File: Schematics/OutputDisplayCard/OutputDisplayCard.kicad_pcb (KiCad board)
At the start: 2 copper layers, 13 parts, among them U1 74LS393, U2 74LS32, U3 74F377, U4 74LS139, U5 74LS245, U6 GLS29EE010, U7 CC56-12CGKWA

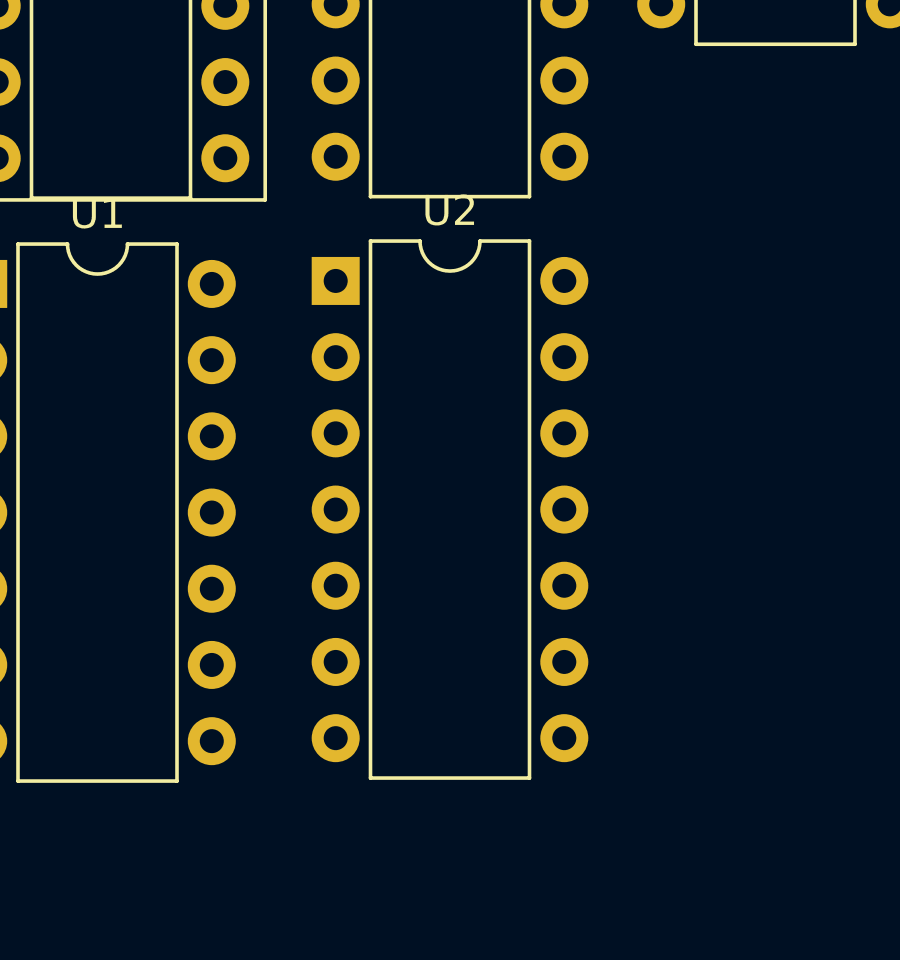
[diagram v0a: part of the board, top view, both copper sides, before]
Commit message: Update schematics for OutputDisplayCard to include the new PI and PO signals.
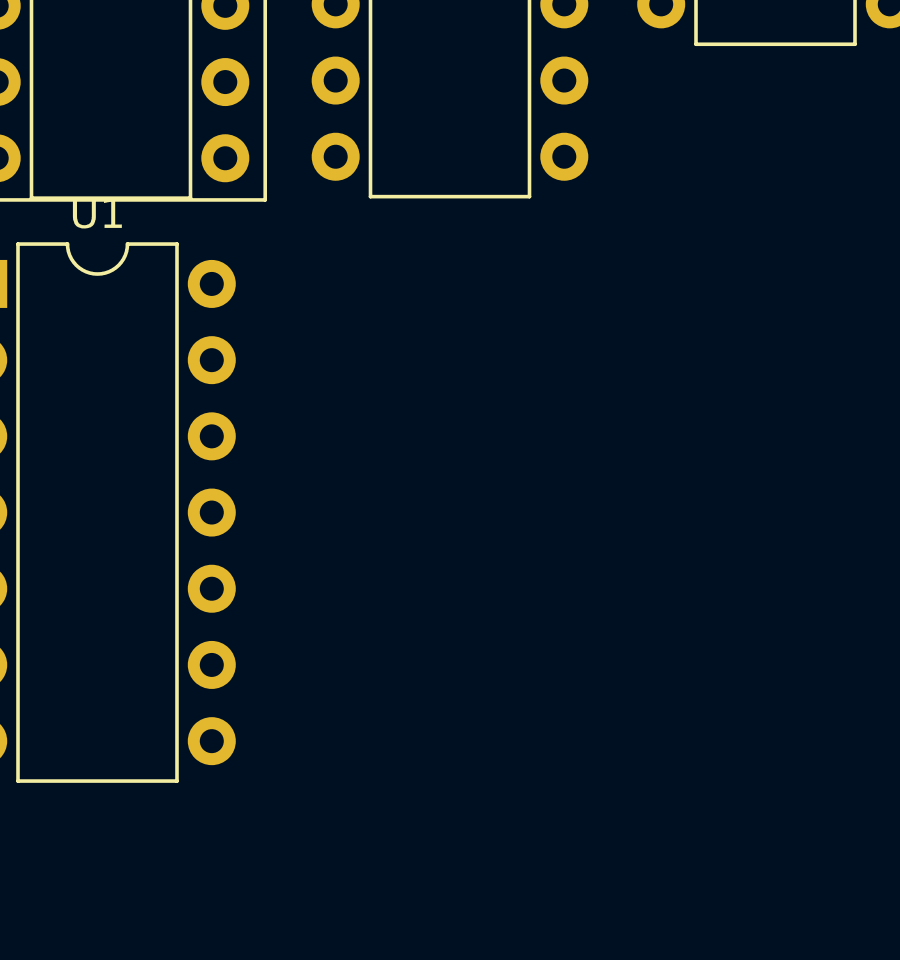
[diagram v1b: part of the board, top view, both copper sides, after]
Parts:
- removed U2: 74LS32, Package_DIP:DIP-14_W7.62mm
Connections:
- U1 pad 1: FixedRateClock -> (no net)
- U1 pad 10: Net-(U1-Pad10) -> (no net)
- U1 pad 11: Net-(U1-Pad11) -> (no net)
- U1 pad 12: Net-(U1-Pad12) -> (no net)
- U1 pad 13: Net-(U1-Pad13) -> (no net)
- U1 pad 8: Net-(U1-Pad8) -> (no net)
- U1 pad 9: Net-(U1-Pad9) -> (no net)
- U3 pad 1: Net-(U2-Pad3) -> (no net)
- U3 pad 11: RegisterClock -> (no net)
- U4 pad 10: Net-(U4-Pad10) -> (no net)
- U4 pad 11: Net-(U4-Pad11) -> (no net)
- U4 pad 12: Net-(U4-Pad12) -> (no net)
- U4 pad 13: Net-(U4-Pad13) -> (no net)
- U4 pad 14: Net-(U4-Pad14) -> (no net)
- U4 pad 15: Net-(U4-Pad15) -> (no net)
- U4 pad 9: Net-(U4-Pad9) -> (no net)
- U5 pad 19: Net-(U2-Pad6) -> (no net)
- U6 pad 1: Net-(U6-Pad1) -> (no net)
- U6 pad 30: Net-(U6-Pad30) -> (no net)
